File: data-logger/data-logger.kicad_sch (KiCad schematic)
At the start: 12 parts, among them J1 AK100, J10 AK100, J11 AK100, J2 USB_A, J3 USB_C_Receptacle_USB2.0_16P, J4 USB_B, J5 USB_B_Micro, J6 AK100, J7 AK100, J8 AK100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

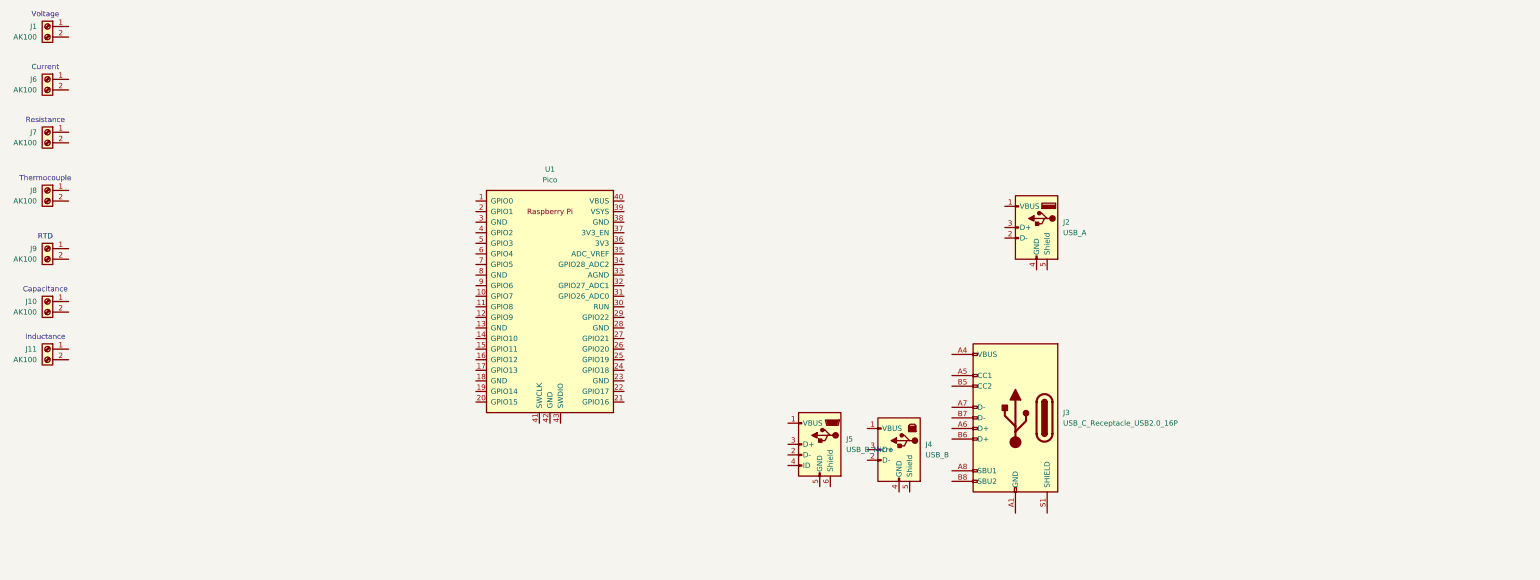
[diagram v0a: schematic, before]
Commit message: changed architecture in schematic
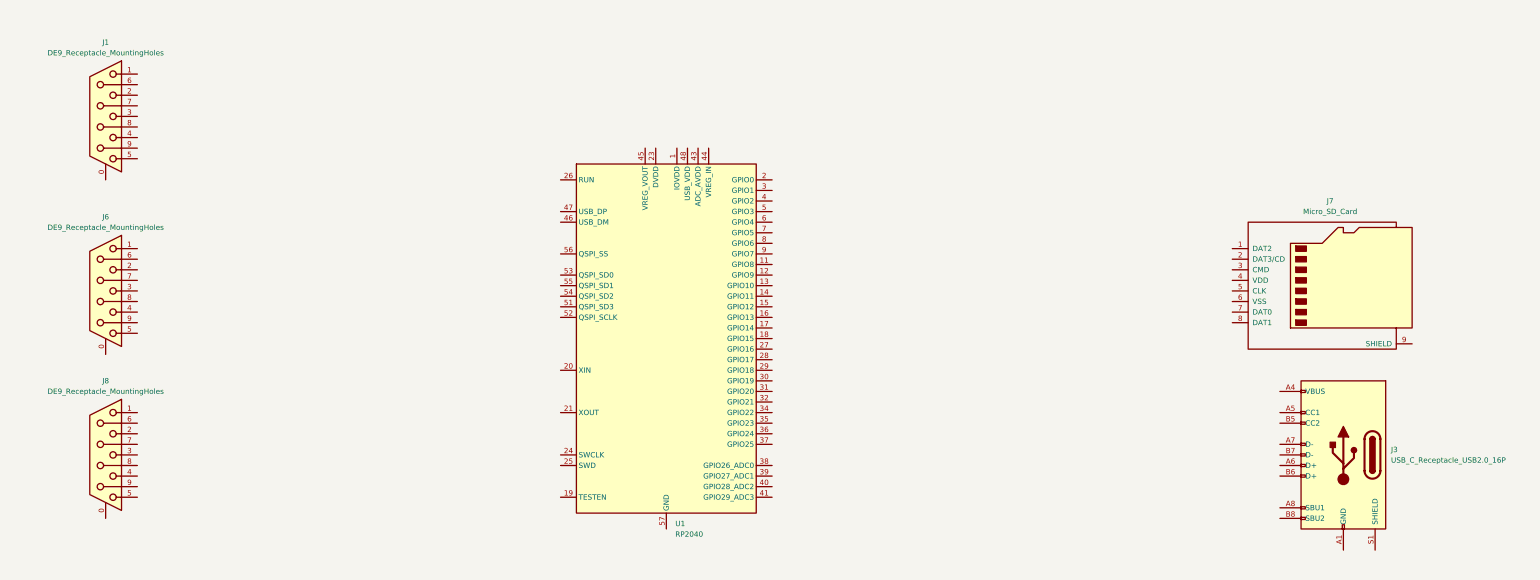
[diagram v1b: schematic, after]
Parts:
- removed J1, J10, J11, J6, J7, J8, J9: AK100, TerminalBlock_Altech:Altech_AK100_1x02_P5.00mm, symbol Connector:Screw_Terminal_01x02
- removed J2: USB_A, Connector_USB:USB_A_Molex_105057_Vertical, symbol Connector:USB_A
- removed J4: USB_B, Connector_USB:USB_B_OST_USB-B1HSxx_Horizontal, symbol Connector:USB_B
- removed J5: USB_B_Micro, Connector_USB:USB_Micro-B_Wuerth_614105150721_Vertical_CircularHoles, symbol Connector:USB_B_Micro
- removed U1: Pico, RPi_Pico:RPi_Pico_SMD_TH, symbol jannett_symbols:Pico
- added J1, J6, J8: DE9_Receptacle_MountingHoles, Connector_Dsub:DSUB-9_Female_Horizontal_P2.77x2.84mm_EdgePinOffset4.94mm_Housed_MountingHolesOffset4.94mm, symbol Connector:DE9_Receptacle_MountingHoles
- added J7: Micro_SD_Card, Connector_Card:microSD_HC_Molex_47219-2001, symbol Connector:Micro_SD_Card
- added U1: RP2040, Package_DFN_QFN:QFN-56-1EP_7x7mm_P0.4mm_EP3.2x3.2mm, symbol MCU_RaspberryPi:RP2040
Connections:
- new net: U1.1 (IOVDD), U1.10 (IOVDD), U1.22 (IOVDD), U1.33 (IOVDD), U1.42 (IOVDD), U1.49 (IOVDD)
- new net: U1.23 (DVDD), U1.50 (DVDD)
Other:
- note removed: "Capacitance"
- note removed: "Current"
- note removed: "Inductance"
- note removed: "RTD"
- note removed: "Resistance"
- note removed: "Thermocouple"
- note removed: "Voltage"
- moved on the sheet: J3

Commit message: schematic
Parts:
- removed J1, J6, J8: DE9_Receptacle_MountingHoles, Connector_Dsub:DSUB-9_Female_Horizontal_P2.77x2.84mm_EdgePinOffset4.94mm_Housed_MountingHolesOffset4.94mm, symbol Connector:DE9_Receptacle_MountingHoles
- removed J3: USB_C_Receptacle_USB2.0_16P, Connector_USB:USB_C_Receptacle_GCT_USB4110, symbol Connector:USB_C_Receptacle_USB2.0_16P
- removed U1: RP2040, Package_DFN_QFN:QFN-56-1EP_7x7mm_P0.4mm_EP3.2x3.2mm, symbol MCU_RaspberryPi:RP2040
- added U1: ATmega328PB-A, Package_QFP:TQFP-32_7x7mm_P0.8mm, symbol MCU_Microchip_ATmega:ATmega328PB-A
- added U2: MAX31855KASA, Package_SO:SOIC-8_3.9x4.9mm_P1.27mm, symbol Sensor_Temperature:MAX31855KASA
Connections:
- new net: U1.21 (GND), U1.5 (GND)
